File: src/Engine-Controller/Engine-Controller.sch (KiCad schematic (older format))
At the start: 4 parts, among them U1 STM32L443VCT6

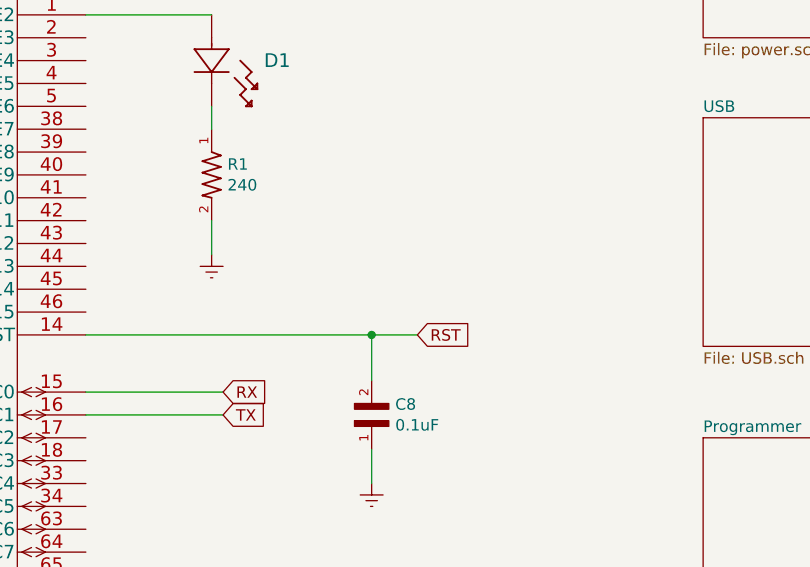
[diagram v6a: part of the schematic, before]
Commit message: Added test points
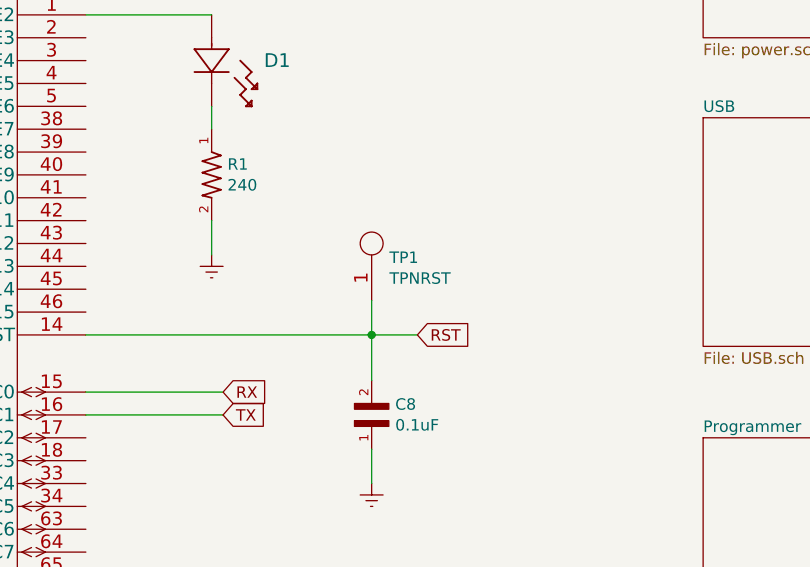
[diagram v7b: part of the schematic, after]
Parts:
- added TP1: TPNRST, symbol Engine-Controller:TP
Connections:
- net RST: now also TP1.1
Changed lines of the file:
@@
 Wire Wire Line
 	6650 3750 6650 3600
+$Comp
+L Engine-Controller:TP TP1
+U 1 1 60E1CD7C
+P 6650 2950
+F 0 "TP1" H 6728 3138 50  0000 L CNN
+F 1 "TPNRST" H 6728 3047 50  0000 L CNN
+F 2 "" H 6650 2950 50  0001 C CNN
+F 3 "" H 6650 2950 50  0001 C CNN
+	1    6650 2950
+	1    0    0    -1
+$EndComp
+Wire Wire Line
+	6650 3100 6650 2950
 $EndSCHEMATC

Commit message: Imported footprints into layout file
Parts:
- TP1: footprint (none) -> Engine-Controller:TP
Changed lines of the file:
@@
 F 0 "TP1" H 6728 3138 50  0000 L CNN
 F 1 "TPNRST" H 6728 3047 50  0000 L CNN
-F 2 "" H 6650 2950 50  0001 C CNN
+F 2 "Engine-Controller:TP" H 6650 2950 50  0001 C CNN
 F 3 "" H 6650 2950 50  0001 C CNN
 	1    6650 2950
